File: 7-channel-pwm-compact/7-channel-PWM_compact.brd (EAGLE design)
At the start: 39 x 26 mm, 18 parts, among them J1 POWER_JACKSLT

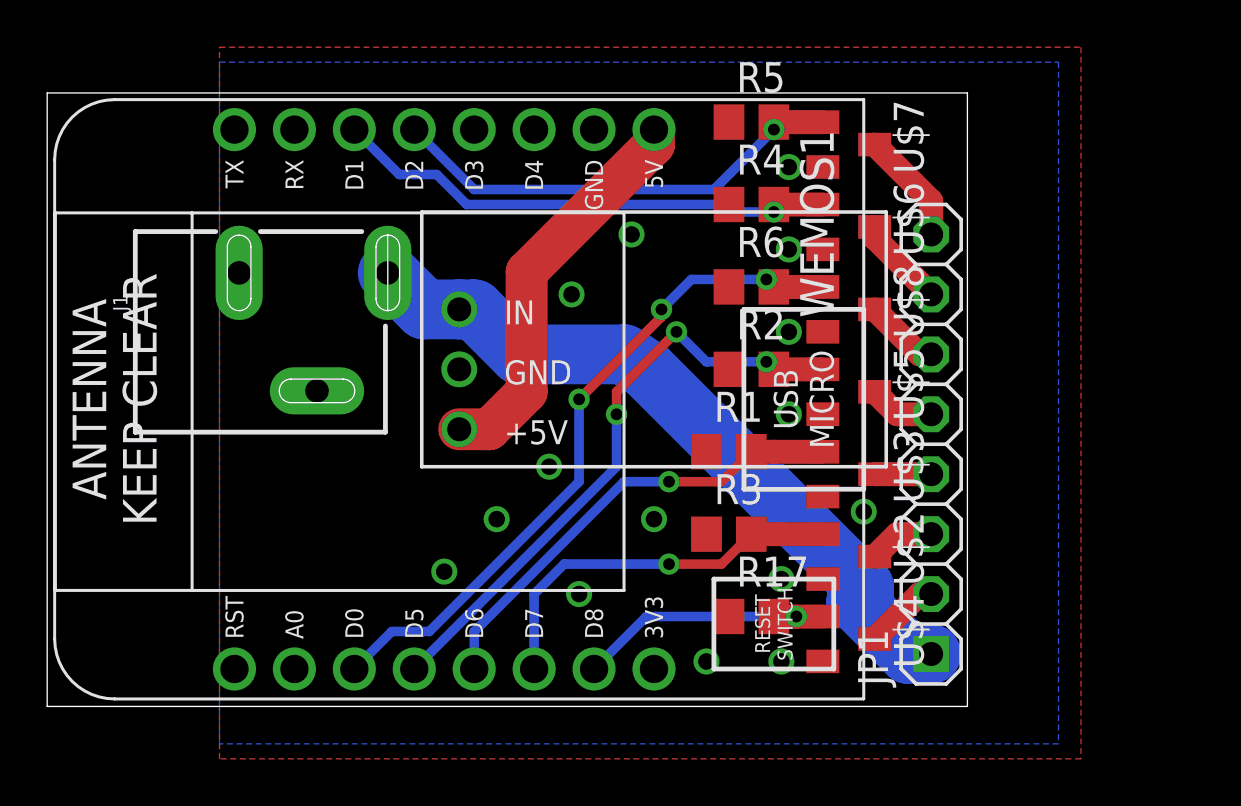
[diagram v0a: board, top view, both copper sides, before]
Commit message: update 7 channel pwm design
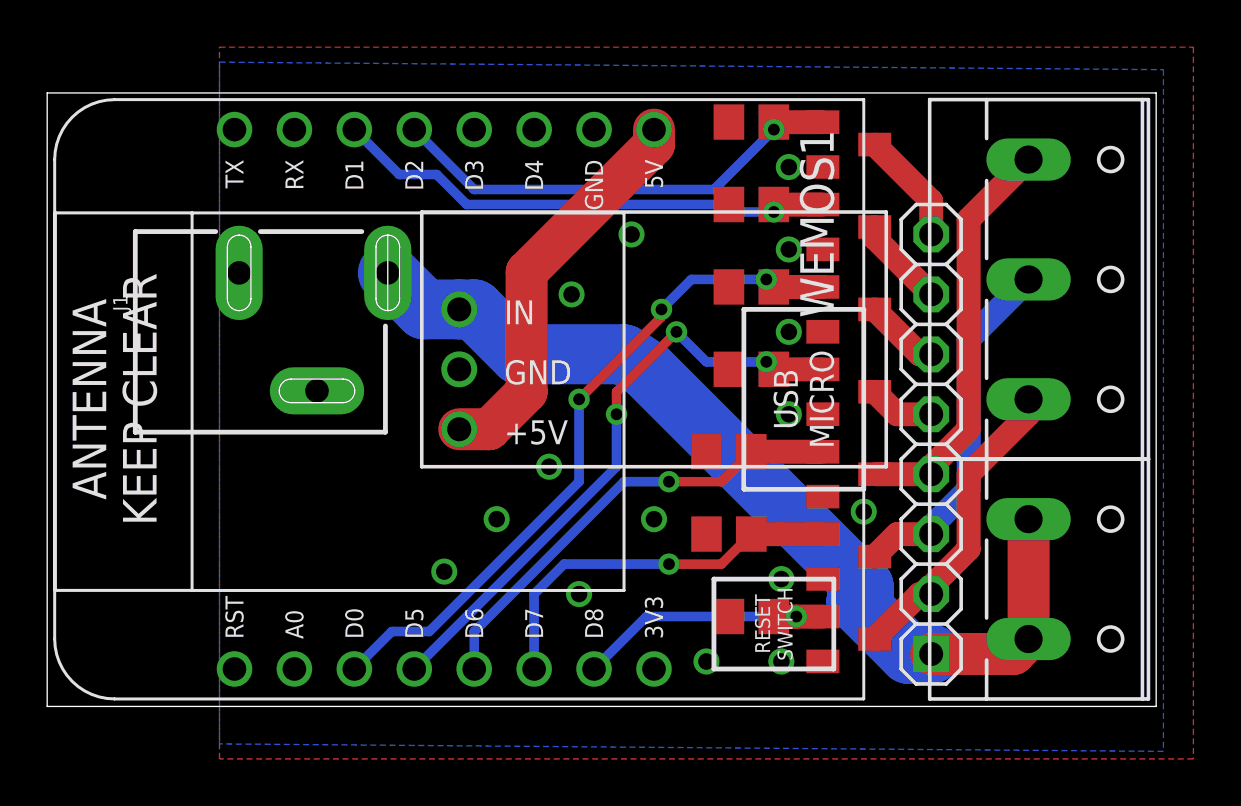
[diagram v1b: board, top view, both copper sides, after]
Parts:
- added X1: (no value), con-wago-508:W237-132
- added X2: (no value), con-wago-508:W237-133
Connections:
- net +12V: now also X1.1, X1.2
- net N$2: now also X2.3
- net N$4: now also X2.2
- net N$5: now also X2.1
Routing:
- net N$5: track 2.39 -> 17.4 mm
- net N$4: track 2.79 -> 15.3 mm
- net N$2: track 3.18 -> 13.1 mm
- net +12V: track 30.5 -> 39.9 mm
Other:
- board size 39 x 26 mm -> 47 x 26 mm
